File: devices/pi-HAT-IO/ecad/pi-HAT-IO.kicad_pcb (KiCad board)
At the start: 2 copper layers, 65 x 56 mm, 19 parts, among them J1 GPIO, J2 5569-04A2, J3 SM04B-SRSS-TB, J4 SM04B-SRSS-TB, Q1 SI4477DY-T1-GE3, Q2 DMMT5401, U1 TLV75733PDBV

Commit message: Adds model for HAT header
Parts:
- added J5: SM04B-SRSS-TB, common:JST_SH_SM04B-SRSS-TB_1x04-1MP_P1.00mm_Horizontal, F.Cu at (141.7, 96.3)
- moved R3 8.45 mm to (145.5, 91.9)
- moved R4 7.90 mm to (145.5, 90.3)
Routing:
- net GND: track 88.9 -> 36.5 mm
- net +3V3: track 78.1 -> 66.6 mm
- net /GPIO3/SCL1: track 66.6 -> 74.6 mm, vias 0 -> 3
- net /GPIO2/SDA1: track 72.3 -> 80.1 mm, vias 0 -> 3
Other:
- board text added: "QWIIC"

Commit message: Conforms all board together
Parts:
- added REF**: OSHW-Logo_7.5x8mm_SilkScreen, Symbol:OSHW-Logo_7.5x8mm_SilkScreen, F.Cu at (132.2, 60.0)
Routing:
- net GND: vias 15 -> 14
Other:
- board text added: "5V 5A"
- board text added: "GLUE RTC BATTERY HERE"
- board text added: "Max 1A@3.3V Total"
- board text added: "Pi 5 HAT - rev A Power Delivery + QWIIC HUB"
- board text added: "RTC"
- board text added: "Use Isolated Standoff"
- board text added: "⚠"

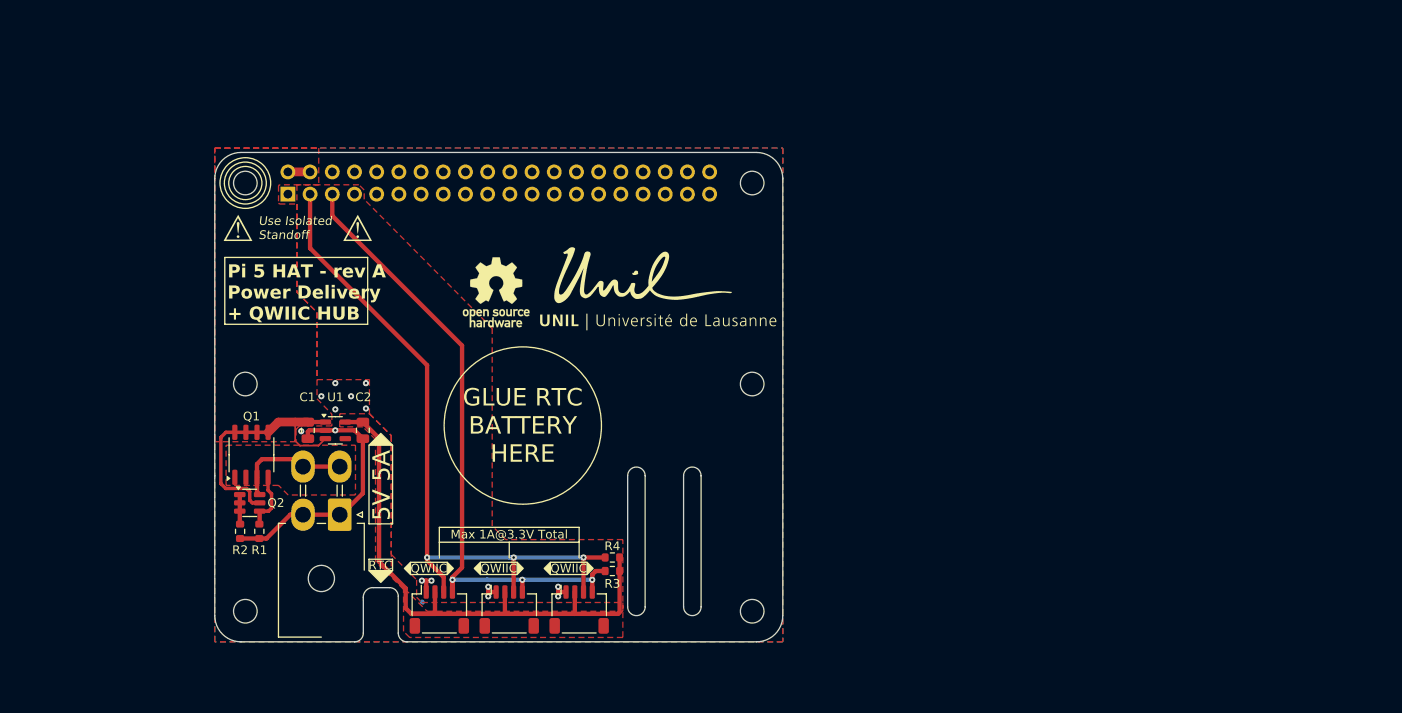
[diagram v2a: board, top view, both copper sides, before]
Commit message: [WIP] Reworks HAT to handle power distribution
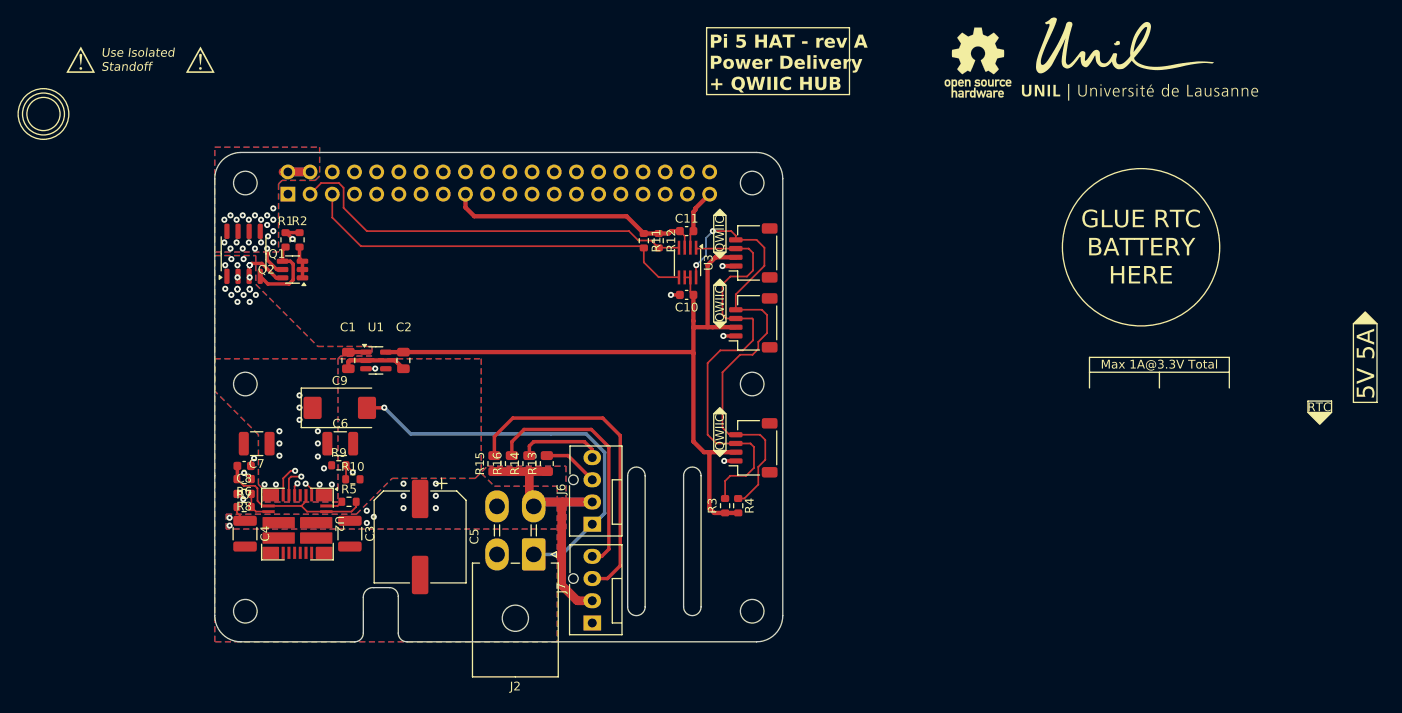
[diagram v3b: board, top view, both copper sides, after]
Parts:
- added C10: 100n, Capacitor_SMD:C_0603_1608Metric, F.Cu at (154.0, 60.3)
- added C11: 100n, Capacitor_SMD:C_0603_1608Metric, F.Cu at (154.0, 53.0)
- added C3: 10uF, Capacitor_SMD:C_1210_3225Metric, F.Cu at (115.5, 87.6)
- added C4: 10uF, Capacitor_SMD:C_1210_3225Metric, F.Cu at (103.5, 87.6)
- added C5: 100u, Capacitor_SMD:CP_Elec_10x12.6, F.Cu at (123.5, 88.0)
- added C6: 47u, Capacitor_SMD:C_1210_3225Metric, F.Cu at (114.4, 77.3)
- added C7: 47u, Capacitor_SMD:C_1210_3225Metric, F.Cu at (104.8, 77.3)
- added C8: 22n, Capacitor_SMD:C_0603_1608Metric, F.Cu at (103.4, 79.9)
- added C9: 330u, Capacitor_Tantalum_SMD:CP_EIA-7343-15_Kemet-W, F.Cu at (114.3, 73.2)
- added J6: 47053-1000, Connector:FanPinHeader_1x04_P2.54mm_Vertical, F.Cu at (143.2, 86.5)
- added J7: 47053-1000, Connector:FanPinHeader_1x04_P2.54mm_Vertical, F.Cu at (143.2, 97.8)
- added R10: 1.37k, Resistor_SMD:R_0603_1608Metric, F.Cu at (115.8, 81.4)
- added R11: 2.2k, Resistor_SMD:R_0603_1608Metric, F.Cu at (149.1, 54.1)
- added R12: 2.2k, Resistor_SMD:R_0603_1608Metric, F.Cu at (150.8, 54.1)
- added R13: 10k, Resistor_SMD:R_0805_2012Metric, F.Cu at (138.0, 79.6)
- added R14: 10k, Resistor_SMD:R_0805_2012Metric, F.Cu at (136.0, 79.6)
- added R15: 10k, Resistor_SMD:R_0805_2012Metric, F.Cu at (132.0, 79.6)
- added R16: 10k, Resistor_SMD:R_0805_2012Metric, F.Cu at (134.0, 79.6)
- added R5: 39k, Resistor_SMD:R_0603_1608Metric, F.Cu at (115.4, 84.0)
- added R6: 48.7k, Resistor_SMD:R_0603_1608Metric, F.Cu at (103.4, 81.4)
- added R7: 68.1k, Resistor_SMD:R_0603_1608Metric, F.Cu at (103.4, 84.6)
- added R8: 8.2k, Resistor_SMD:R_0603_1608Metric, F.Cu at (103.4, 83.1)
- added R9: 10k, Resistor_SMD:R_0603_1608Metric, F.Cu at (114.2, 79.8)
- added U2: PMU8418, common:PMU8000, F.Cu at (109.5, 86.5)
- added U3: TCA9406DC, Package_SO:SSOP-8_2.95x2.8mm_P0.65mm, F.Cu at (154.1, 56.6)
- R3, R4: value 10k -> 2.2k
- moved REF** 61.1 mm to (187.3, 33.7)
- moved J5 45.4 mm to (161.6, 55.5), turned to 90 degrees
- moved J4 43.1 mm to (161.6, 63.5), turned to 90 degrees
- moved J3 40.4 mm to (161.6, 77.8), turned to 90 degrees
- moved R2 34.0 mm to (109.7, 54.0), turned to 90 degrees
- moved R1 33.5 mm to (108.1, 54.0), turned to 90 degrees
- moved Q2 27.1 mm to (108.9, 57.4), turned to 180 degrees
- moved Q1 23.0 mm to (103.3, 55.6)
- moved J2 22.7 mm to (136.5, 90.0)
- moved R4 15.6 mm to (159.9, 84.4), turned to 90 degrees
- moved R3 14.9 mm to (158.4, 84.4), turned to 90 degrees
- moved C2 9.25 mm to (121.6, 67.8)
- moved U1 9.25 mm to (118.4, 67.8)
- moved C1 9.25 mm to (115.3, 67.8)
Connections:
- J1 pad 17: unconnected-(J1-Pin_17-Pad17) -> +3V3_PI
- J1 pad 2: +5V -> +5V_PI
- J1 pad 4: +5V -> +5V_PI
- J2 pad 3: /VIN -> +12V
- J2 pad 4: /VIN -> +12V
- J3 pad 3: /GPIO2/SDA1 -> /SDA
- J3 pad 4: /GPIO3/SCL1 -> /SCL
- J4 pad 3: /GPIO2/SDA1 -> /SDA
- J4 pad 4: /GPIO3/SCL1 -> /SCL
- J5 pad 3: /GPIO2/SDA1 -> /SDA
- J5 pad 4: /GPIO3/SCL1 -> /SCL
- Q1 pad 1: /VIN -> +5V
- Q1 pad 3: +5V -> +5V_PI
- Q2 pad 5: +5V -> +5V_PI
- Q2 pad 6: /VIN -> +5V
- R3 pad 2: /GPIO3/SCL1 -> /SDA
- R4 pad 2: /GPIO2/SDA1 -> /SCL
- U1 pad 3: +5V -> /3V3_EN
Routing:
- net /SCL: track 0.00 -> 55.1 mm, vias 0 -> 2
- net /SDA: track 0.00 -> 51.2 mm
- net +12V: track 0.00 -> 39.8 mm, vias 0 -> 11
- net /TACHO1: track 0.00 -> 37.0 mm
- net GND: track 36.5 -> 69.9 mm, vias 14 -> 7
- net /GPIO2/SDA1: track 80.1 -> 47.2 mm, vias 3 -> 0
- net +3V3_PI: track 0.00 -> 29.5 mm
- net /GPIO3/SCL1: track 74.6 -> 46.2 mm, vias 3 -> 0
- net /FAN1: track 0.00 -> 28.0 mm
- net +5V: track 32.7 -> 7.84 mm, vias 0 -> 32
- net /3V3_EN: track 0.00 -> 24.5 mm, vias 0 -> 2
- net /AGND: track 0.00 -> 19.8 mm
- net +3V3: track 66.6 -> 85.7 mm
- net /VIN: track 13.9 -> 0.00 mm
- net /FB: track 0.00 -> 10.9 mm, vias 0 -> 2
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- added copper zone on B.Cu, net +12V
- added copper zone on F.Cu, net +12V
- added copper zone on B.Cu, net +5V
- added copper zone on B.Cu, net +5V_PI
- added copper zone on F.Cu, net +5V_PI
- added copper zone on In1.Cu, net +5V_PI
- added copper zone on In2.Cu, net +5V_PI
- added copper zone on In1.Cu, net GND
- added copper zone on In2.Cu, net GND
- removed copper zone on F.Cu, net +3V3
- removed copper zone on F.Cu, net /VIN
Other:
- copper layers 2 -> 4

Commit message: Reworks HAT to handle power delivery and fan control
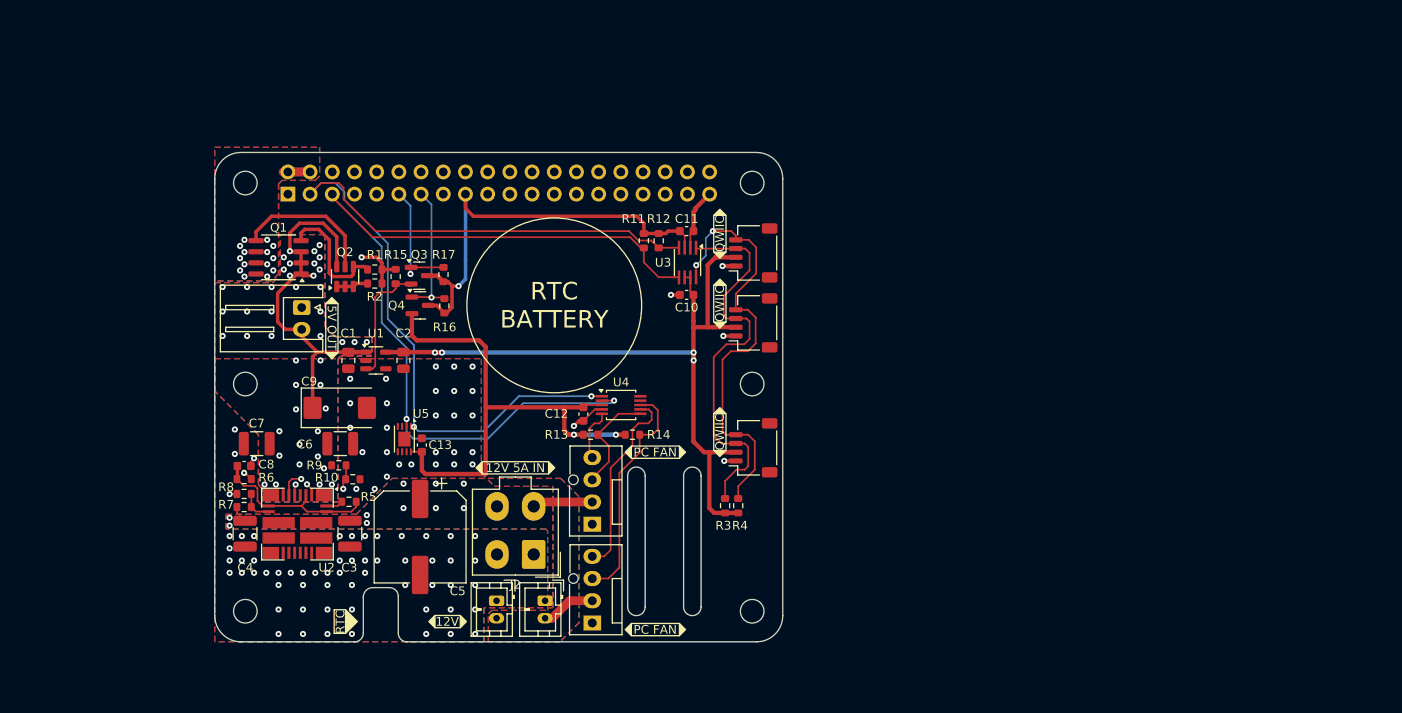
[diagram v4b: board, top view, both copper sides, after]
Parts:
- added C12: 100n, Capacitor_SMD:C_0603_1608Metric, F.Cu at (142.2, 73.9)
- added C13: 100n, Capacitor_SMD:C_0603_1608Metric, F.Cu at (123.7, 77.5)
- added J10: JST XH, Connector_JST:JST_XH_S2B-XH-A_1x02_P2.50mm_Horizontal, F.Cu at (110.0, 61.8)
- added J8: JST PH, Connector_JST:JST_PH_B2B-PH-K_1x02_P2.00mm_Vertical, F.Cu at (137.8, 95.3)
- added J9: JST PH, Connector_JST:JST_PH_B2B-PH-K_1x02_P2.00mm_Vertical, F.Cu at (132.2, 95.3)
- added Q3: DMG2305UX, Package_TO_SOT_SMD:SOT-23, F.Cu at (123.4, 58.1)
- added Q4: DMG2305UX, Package_TO_SOT_SMD:SOT-23, F.Cu at (123.5, 61.5)
- added R17: 10k, Resistor_SMD:R_0603_1608Metric, F.Cu at (126.2, 58.0)
- added U4: EMC2302, Package_SO:MSOP-10_3x3mm_P0.5mm, F.Cu at (146.5, 72.9)
- added U5: MCP9804_DFN, Package_DFN_QFN:DFN-8-1EP_3x2mm_P0.5mm_EP1.7x1.4mm, F.Cu at (121.7, 76.8)
- J2: value 5569-04A2 -> Mini-Fit Jr; footprint common:Molex_Mini-Fit_Jr_5569-04A2_2x02_P4.20mm_Horizontal -> common:Molex_Mini-Fit_Jr_5566-04A_2x02_P4.20mm_Vertical
- J3, J4, J5: value SM04B-SRSS-TB -> JST SH
- J6, J7: value 47053-1000 -> PC FAN HEADER
- R13, R14, R15, R16: footprint Resistor_SMD:R_0805_2012Metric -> Resistor_SMD:R_0603_1608Metric
- REF**: moved to B.Cu
- moved REF** 70.5 mm to (126.0, 68.4), turned to 180 degrees
- moved R15 24.2 mm to (120.7, 58.2)
- moved R16 19.6 mm to (126.3, 61.5)
- moved R14 12.3 mm to (147.8, 76.3), turned to 0 degrees
- moved R1 10.8 mm to (118.3, 57.4), turned to 0 degrees
- moved R2 9.96 mm to (118.3, 59.0), turned to 0 degrees
- moved Q2 6.07 mm to (114.9, 58.2), turned to 90 degrees
- moved R13 5.99 mm to (143.0, 76.3), turned to 0 degrees
- moved Q1 4.02 mm to (107.3, 56.0), turned to 180 degrees
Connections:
- net /TACHO0 renamed /TACH0
- C10 pad 1: +3V3 -> +3V3_OUT
- C2 pad 1: +3V3 -> +3V3_OUT
- J1 pad 11: /GPIO17 -> /GPIO17/~{3V3_OUT_EN}
- J1 pad 13: /GPIO27 -> /GPIO27/~{3V3_EN}
- J3 pad 2: +3V3 -> +3V3_OUT
- J4 pad 2: +3V3 -> +3V3_OUT
- J5 pad 2: +3V3 -> +3V3_OUT
- J7 pad 3: /TACHO1 -> /TACH1
- R13 pad 1: +12V -> +3V3
- R14 pad 1: +12V -> +3V3
- R14 pad 2: /FAN0 -> /TACH1
- R15 pad 1: +12V -> /3V3_EN
- R15 pad 2: /TACHO1 -> GND
- R16 pad 1: +12V -> +3V3_PI
- R16 pad 2: /FAN1 -> /GPIO27/~{3V3_EN}
- R3 pad 1: +3V3 -> +3V3_OUT
- R4 pad 1: +3V3 -> +3V3_OUT
- U1 pad 5: +3V3 -> +3V3_OUT
- U2 pad 7: /3V3_EN -> /5V_GOOD
- U3 pad 6: +3V3 -> +3V3_OUT
- U3 pad 7: +3V3 -> +3V3_OUT
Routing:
- net +3V3_OUT: track 0.00 -> 87.3 mm, vias 0 -> 4
- net /GPIO2/SDA1: track 47.2 -> 105.4 mm, vias 0 -> 2
- net /GPIO3/SCL1: track 46.2 -> 103.7 mm, vias 0 -> 2
- net GND: track 69.9 -> 23.7 mm, vias 7 -> 93
- net /TACHO1: track 37.0 -> 0.00 mm
- net +5V: track 7.84 -> 42.7 mm, vias 32 -> 44
- net /TACH1: track 0.00 -> 26.6 mm
- net +12V: track 39.8 -> 15.1 mm, vias 11 -> 10
- net +3V3: track 85.7 -> 61.2 mm, vias 0 -> 2
- net +3V3_PI: track 29.5 -> 51.0 mm, vias 0 -> 1
- net /GPIO27/~{3V3_EN}: track 0.00 -> 16.1 mm, vias 0 -> 1
- net /GPIO17/~{3V3_OUT_EN}: track 0.00 -> 14.2 mm, vias 0 -> 1
- net +5V_PI: track 9.16 -> 22.0 mm, vias 22 -> 14
- net /3V3_EN: track 24.5 -> 14.6 mm, vias 2 -> 0
- net /SS: track 10.7 -> 19.1 mm
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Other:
- board text added: "12V"
- board text added: "12V 5A IN"
- board text added: "5V OUT"
- board text added: "PC FAN"
- board text added: "Pi 5 HAT - rev A 12V Power Delivery QWIIC HUB FAN CTRL"
- board text added: "RTC BATTERY"
- board text removed: "5V 5A"
- board text removed: "GLUE RTC BATTERY HERE"
- board text removed: "Max 1A@3.3V Total"
- board text removed: "Pi 5 HAT - rev A Power Delivery + QWIIC HUB"
- board text removed: "Use Isolated Standoff"
- board text removed: "⚠"

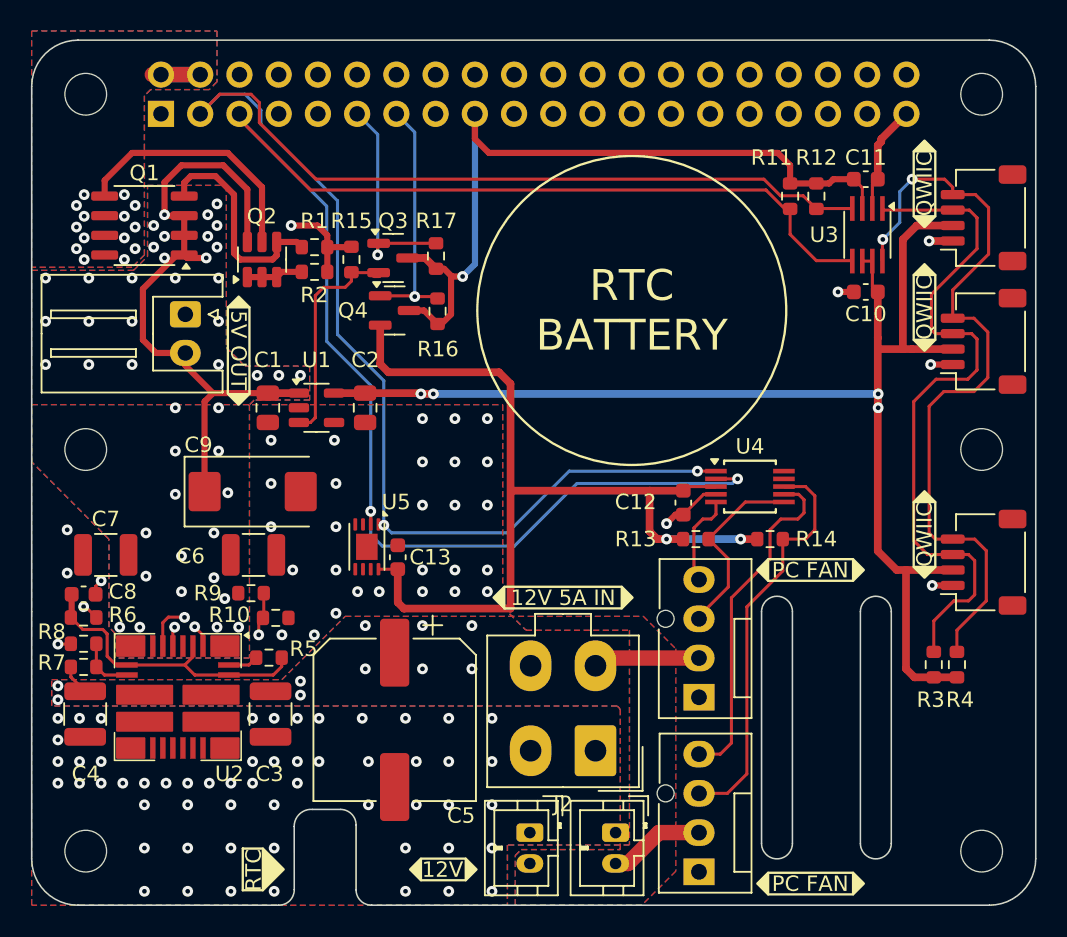
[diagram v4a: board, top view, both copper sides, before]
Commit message: Corrects PCB for production'
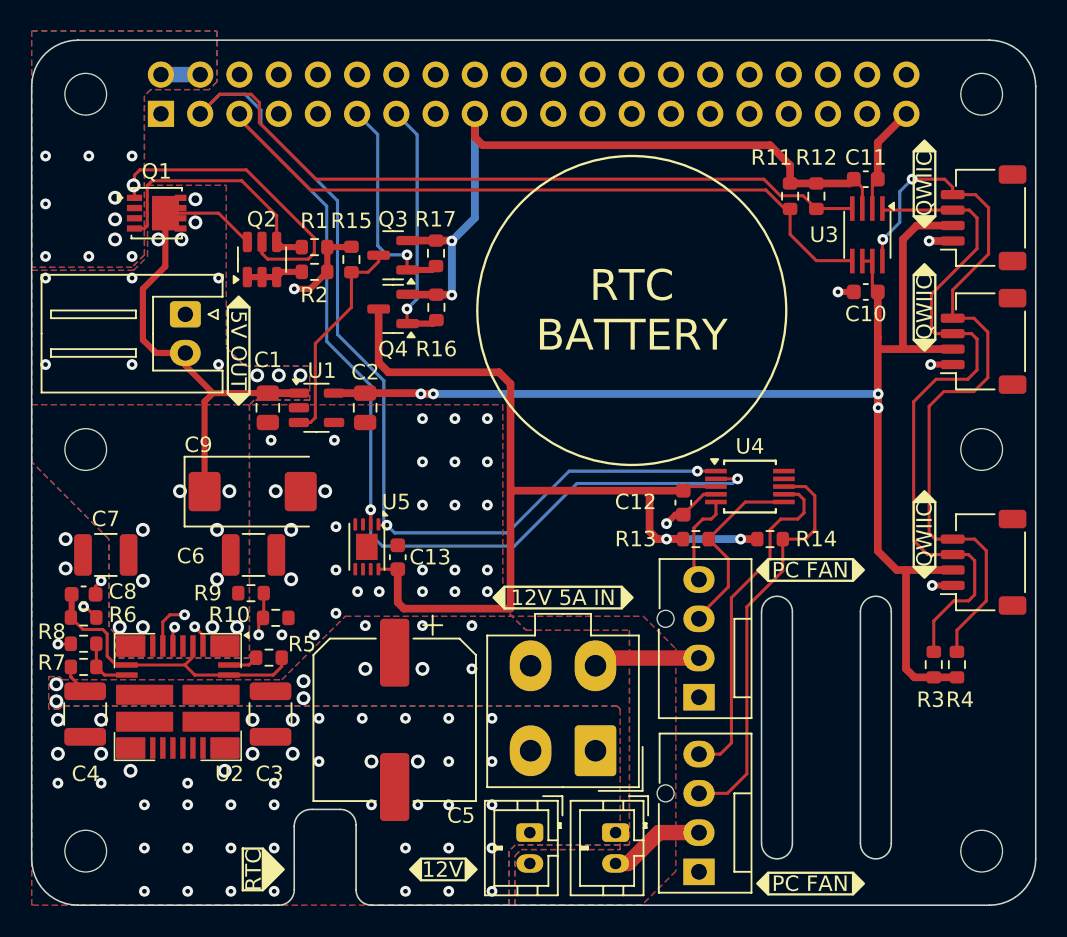
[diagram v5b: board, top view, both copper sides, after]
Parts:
- added REF**: KiCad-Logo2_5mm_SilkScreen, Symbol:KiCad-Logo2_5mm_SilkScreen, B.Cu at (114.1, 73.7)
- Q1: value SI4477DY-T1-GE3 -> SiS435DNT; footprint Package_SO:SO-8_3.9x4.9mm_P1.27mm -> Package_SO:Vishay_PowerPAK_1212-8_Single
- Q2: value DMMT5401 -> DMMT5401-7-F
- R1: value 10k -> 48.7k
- U3: value TCA9406DC -> TCA9406DCTR
- moved REF** 4.17 mm to (126.0, 72.6)
- moved Q1 1.13 mm to (108.1, 55.2), turned to 0 degrees
- moved R16 0.26 mm to (126.2, 61.3), turned to -90 degrees
- moved Q3 0.18 mm to (123.4, 57.9), turned to 180 degrees
- moved R17 0.18 mm to (126.2, 57.8), turned to -90 degrees
- moved Q4 0.14 mm to (123.4, 61.4), turned to 180 degrees
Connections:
- Q1 pad 1: +5V -> +5V_PI
- Q1 pad 2: /E_L -> +5V_PI
- Q3 pad 2: /3V3_EN -> +3V3_PI
- Q3 pad 3: +3V3_PI -> /3V3_EN
- Q4 pad 2: +3V3 -> +3V3_PI
- Q4 pad 3: +3V3_PI -> +3V3
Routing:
- net +5V: track 42.7 -> 33.5 mm, vias 44 -> 23
- net +3V3_PI: track 51.0 -> 48.4 mm, vias 1 -> 2
- net /E_L: track 14.2 -> 16.4 mm
- net +3V3: track 61.2 -> 62.3 mm
- net +5V_PI: track 22.0 -> 23.0 mm, vias 14 -> 11
- net GND: track 23.7 -> 22.9 mm, vias 93 -> 83
- net /3V3_EN: track 14.6 -> 14.0 mm
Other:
- board text added: "Licensed under CERN-OHL-S v2"
- board text added: "Pi 5 HAT - Rev A 12V Power Delivery QWIIC HUB FAN CTRL"
- board text removed: "Pi 5 HAT - rev A 12V Power Delivery QWIIC HUB FAN CTRL"
